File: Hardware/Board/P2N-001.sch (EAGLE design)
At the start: 36 parts, among them IC1 4053N, IC2 LTC485N, IC3 74LS07N, IC4 LTC485N, K1 G5V1, T1 2SC1815

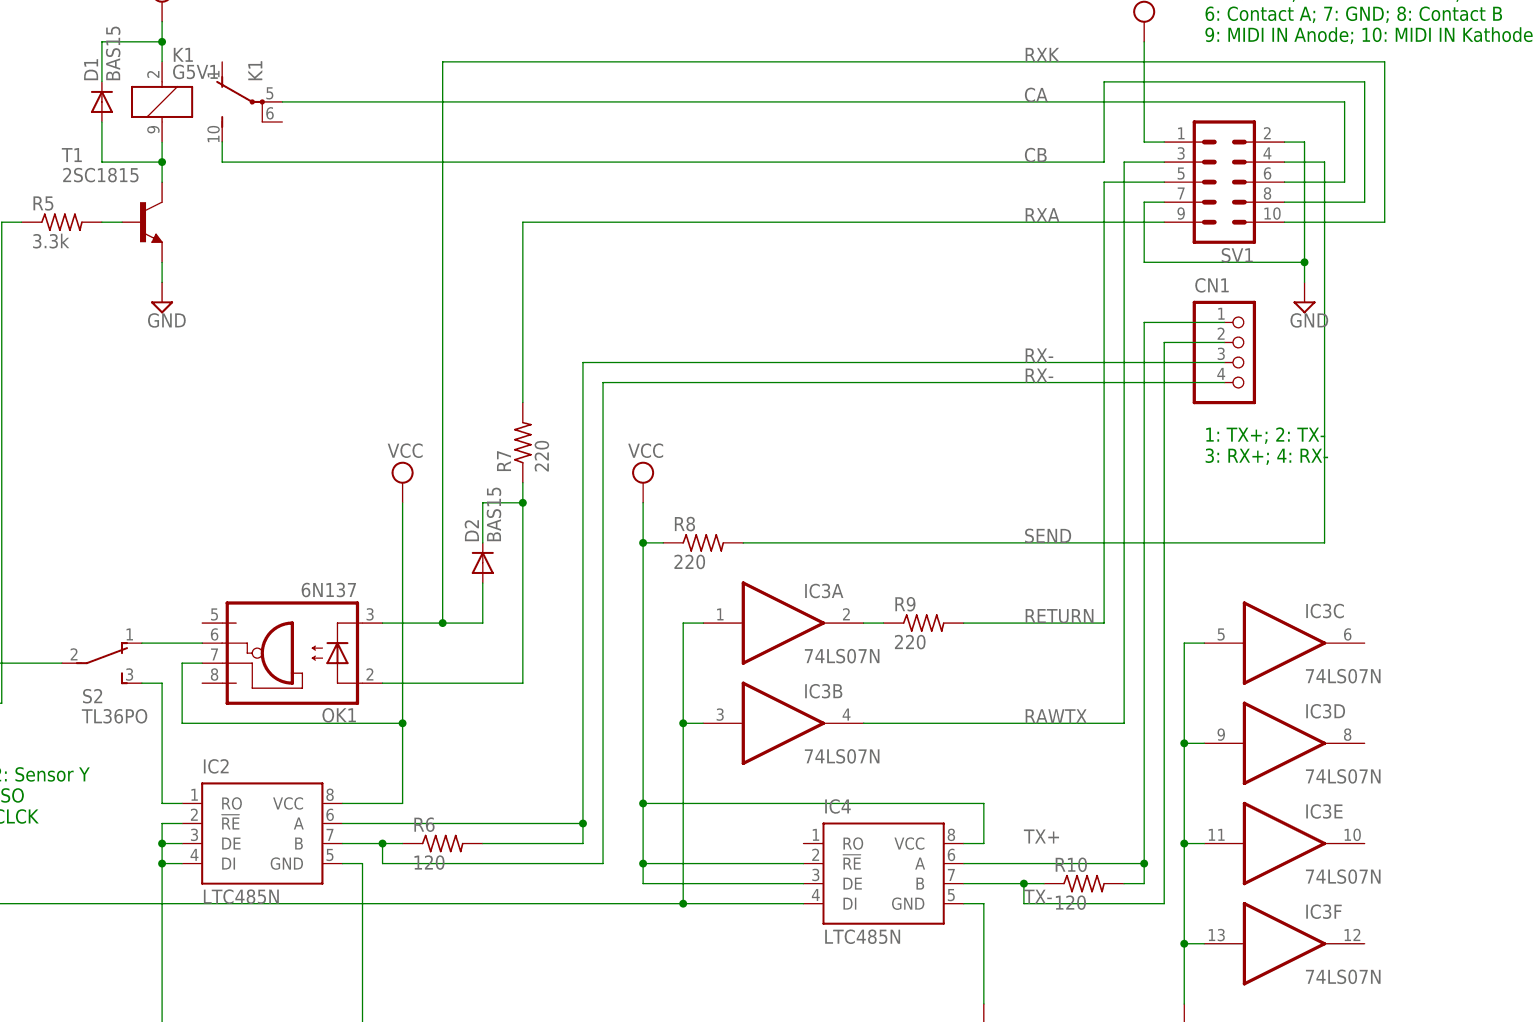
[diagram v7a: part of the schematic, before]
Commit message: Added MIDI THRU function.
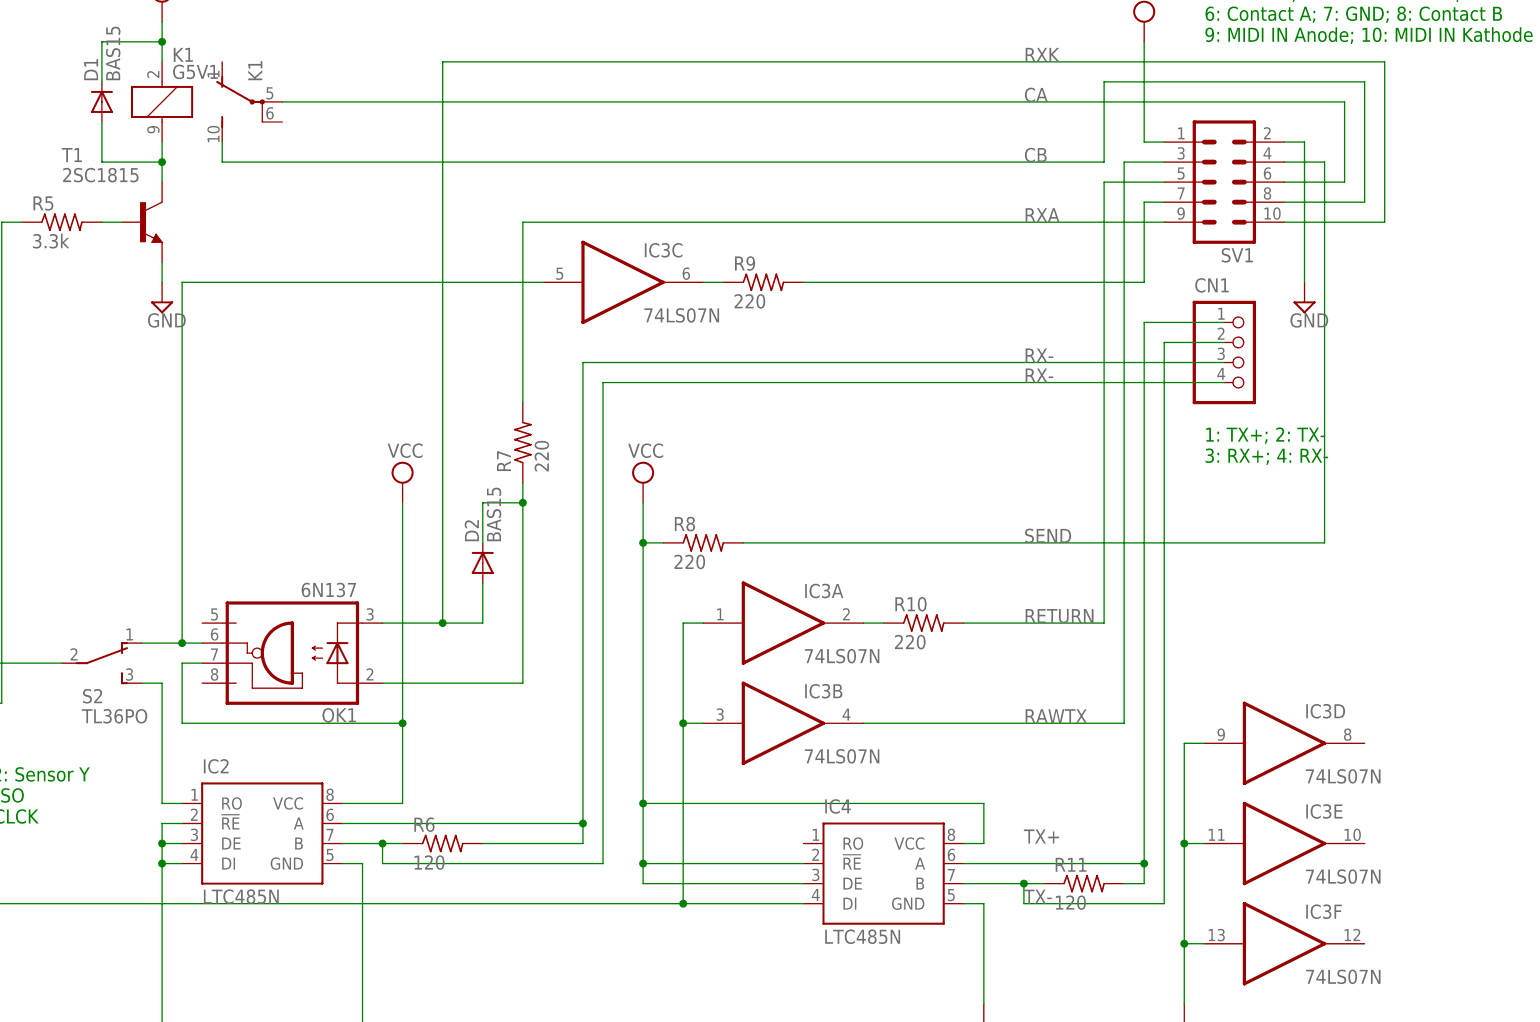
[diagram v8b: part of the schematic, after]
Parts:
- added R11: 120, resistor:R-US_0204/5
- JP4: device pinhead:PINHD-1X2 -> pinhead:PINHD-1X2/90
- R10: value 120 -> 220
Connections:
- new net N$3: IC3C.O, R9.1
- new net N$4: R9.2, SV1.7
- net GND: no longer IC3C.I, SV1.7
- net MIDIRX: now also IC3C.I
- net N$2: now also R10.1; no longer R9.1
- net RETURN: now also R10.2; no longer R9.2
- net TX+: now also R11.2; no longer R10.2
- net TX-: now also R11.1; no longer R10.1
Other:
- moved on the sheet: IC3C, R10, R9
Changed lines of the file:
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@@
 </classes>
 <parts>
-<part name="R9" library="resistor" deviceset="R-US_" device="0204/5" value="220"/>
+<part name="R10" library="resistor" deviceset="R-US_" device="0204/5" value="220"/>
 <part name="R7" library="resistor" deviceset="R-US_" device="0204/5" value="220"/>
 <part name="IC3" library="74xx-us" deviceset="74*07" device="N" technology="LS"/>
@@
 <part name="SUPPLY16" library="supply2" deviceset="GND" device=""/>
 <part name="R6" library="resistor" deviceset="R-US_" device="0204/5" value="120"/>
-<part name="R10" library="resistor" deviceset="R-US_" device="0204/5" value="120"/>
+<part name="R11" library="resistor" deviceset="R-US_" device="0204/5" value="120"/>
 <part name="SUPPLY19" library="supply2" deviceset="VCC" device=""/>
 <part name="SUPPLY22" library="supply2" deviceset="VCC" device=""/>
@@
 <part name="S2" library="switch" deviceset="TL36PO" device=""/>
 <part name="JP5" library="pinhead" deviceset="PINHD-2X3" device=""/>
-<part name="JP4" library="pinhead" deviceset="PINHD-1X2" device=""/>
+<part name="JP4" library="pinhead" deviceset="PINHD-1X2" device="/90"/>
 <part name="S1" library="switch-dil" deviceset="DS01E" device=""/>
 <part name="SUPPLY8" library="supply2" deviceset="GND" device=""/>
+<part name="R9" library="resistor" deviceset="R-US_" device="0204/5" value="220"/>
 </parts>
 <sheets>
@@
 </plain>
 <instances>
-<instance part="R9" gate="G$1" x="248.92" y="60.96"/>
+<instance part="R10" gate="G$1" x="248.92" y="60.96"/>
 <instance part="R7" gate="G$1" x="198.12" y="83.82" rot="R90"/>
 <instance part="IC3" gate="A" x="231.14" y="60.96"/>
@@
 <instance part="SUPPLY16" gate="GND" x="256.54" y="10.16"/>
 <instance part="R6" gate="G$1" x="187.96" y="33.02"/>
-<instance part="R10" gate="G$1" x="269.24" y="27.94"/>
+<instance part="R11" gate="G$1" x="269.24" y="27.94"/>
 <instance part="SUPPLY19" gate="G$1" x="271.78" y="180.34"/>
 <instance part="SUPPLY22" gate="G$1" x="279.4" y="180.34"/>
@@
 <instance part="MC1" gate="G$1" x="58.42" y="50.8" rot="R270"/>
 <instance part="IC3" gate="B" x="231.14" y="48.26"/>
-<instance part="IC3" gate="C" x="294.64" y="58.42"/>
+<instance part="IC3" gate="C" x="210.82" y="104.14"/>
 <instance part="VDD2" gate="G$1" x="7.62" y="40.64"/>
 <instance part="SUPPLY9" gate="GND" x="114.3" y="93.98"/>
@@
 <instance part="S1" gate="1" x="83.82" y="15.24" rot="R270"/>
 <instance part="SUPPLY8" gate="GND" x="91.44" y="7.62"/>
+<instance part="R9" gate="G$1" x="228.6" y="104.14"/>
 </instances>
 <busses>
@@
 <junction x="281.94" y="33.02"/>
 <junction x="281.94" y="20.32"/>
-<pinref part="IC3" gate="C" pin="I"/>
-<wire x1="284.48" y1="58.42" x2="281.94" y2="58.42" width="0.1524" layer="91"/>
-<wire x1="281.94" y1="58.42" x2="281.94" y2="45.72" width="0.1524" layer="91"/>
-<junction x="281.94" y="45.72"/>
 </segment>
 <segment>
@@
 <pinref part="SUPPLY29" gate="GND" pin="GND"/>
 <wire x1="294.64" y1="121.92" x2="297.18" y2="121.92" width="0.1524" layer="91"/>
-<wire x1="297.18" y1="121.92" x2="297.18" y2="106.68" width="0.1524" layer="91"/>
-<pinref part="SV1" gate="1" pin="7"/>
-<wire x1="297.18" y1="106.68" x2="297.18" y2="104.14" width="0.1524" layer="91"/>
-<wire x1="279.4" y1="114.3" x2="276.86" y2="114.3" width="0.1524" layer="91"/>
-<wire x1="276.86" y1="114.3" x2="276.86" y2="106.68" width="0.1524" layer="91"/>
-<wire x1="276.86" y1="106.68" x2="297.18" y2="106.68" width="0.1524" layer="91"/>
-<junction x="297.18" y="106.68"/>
+<wire x1="297.18" y1="121.92" x2="297.18" y2="104.14" width="0.1524" layer="91"/>
 </segment>
 <segment>
@@
 <segment>
 <pinref part="OK1" gate="A" pin="VO"/>
-<wire x1="149.86" y1="58.42" x2="157.48" y2="58.42" width="0.1524" layer="91"/>
+<wire x1="149.86" y1="58.42" x2="154.94" y2="58.42" width="0.1524" layer="91"/>
 <pinref part="S2" gate="BEF1" pin="O"/>
+<wire x1="154.94" y1="58.42" x2="157.48" y2="58.42" width="0.1524" layer="91"/>
+<wire x1="154.94" y1="58.42" x2="154.94" y2="104.14" width="0.1524" layer="91"/>
+<pinref part="IC3" gate="C" pin="I"/>
+<wire x1="154.94" y1="104.14" x2="200.66" y2="104.14" width="0.1524" layer="91"/>
+<junction x="154.94" y="58.42"/>
 </segment>
 </net>
@@
 <segment>
 <pinref part="IC3" gate="A" pin="O"/>
-<pinref part="R9" gate="G$1" pin="1"/>
+<pinref part="R10" gate="G$1" pin="1"/>
 <wire x1="241.3" y1="60.96" x2="243.84" y2="60.96" width="0.1524" layer="91"/>
 </segment>
@@
 <net name="TX+" class="0">
 <segment>
-<pinref part="R10" gate="G$1" pin="2"/>
+<pinref part="R11" gate="G$1" pin="2"/>
 <wire x1="276.86" y1="27.94" x2="274.32" y2="27.94" width="0.1524" layer="91"/>
 <pinref part="IC4" gate="G$1" pin="A"/>
@@
 <segment>
 <pinref part="IC4" gate="G$1" pin="B"/>
-<pinref part="R10" gate="G$1" pin="1"/>
+<pinref part="R11" gate="G$1" pin="1"/>
 <wire x1="254" y1="27.94" x2="261.62" y2="27.94" width="0.1524" layer="91"/>
 <pinref part="CN1" gate="G$1" pin="2"/>
@@
 <net name="RETURN" class="0">
 <segment>
-<pinref part="R9" gate="G$1" pin="2"/>
+<pinref part="R10" gate="G$1" pin="2"/>
 <wire x1="254" y1="60.96" x2="271.78" y2="60.96" width="0.1524" layer="91"/>
 <wire x1="271.78" y1="60.96" x2="271.78" y2="116.84" width="0.1524" layer="91"/>
@@
 </segment>
 </net>
+<net name="N$3" class="0">
+<segment>
+<pinref part="IC3" gate="C" pin="O"/>
+<pinref part="R9" gate="G$1" pin="1"/>
+<wire x1="223.52" y1="104.14" x2="220.98" y2="104.14" width="0.1524" layer="91"/>
+</segment>
+</net>
+<net name="N$4" class="0">
+<segment>
+<pinref part="R9" gate="G$1" pin="2"/>
+<wire x1="233.68" y1="104.14" x2="276.86" y2="104.14" width="0.1524" layer="91"/>
+<wire x1="276.86" y1="104.14" x2="276.86" y2="114.3" width="0.1524" layer="91"/>
+<pinref part="SV1" gate="1" pin="7"/>
+<wire x1="276.86" y1="114.3" x2="279.4" y2="114.3" width="0.1524" layer="91"/>
+</segment>
+</net>
